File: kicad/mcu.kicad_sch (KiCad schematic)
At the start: 1 part, among them U12 ESP32-S3-WROOM-1-N8R2

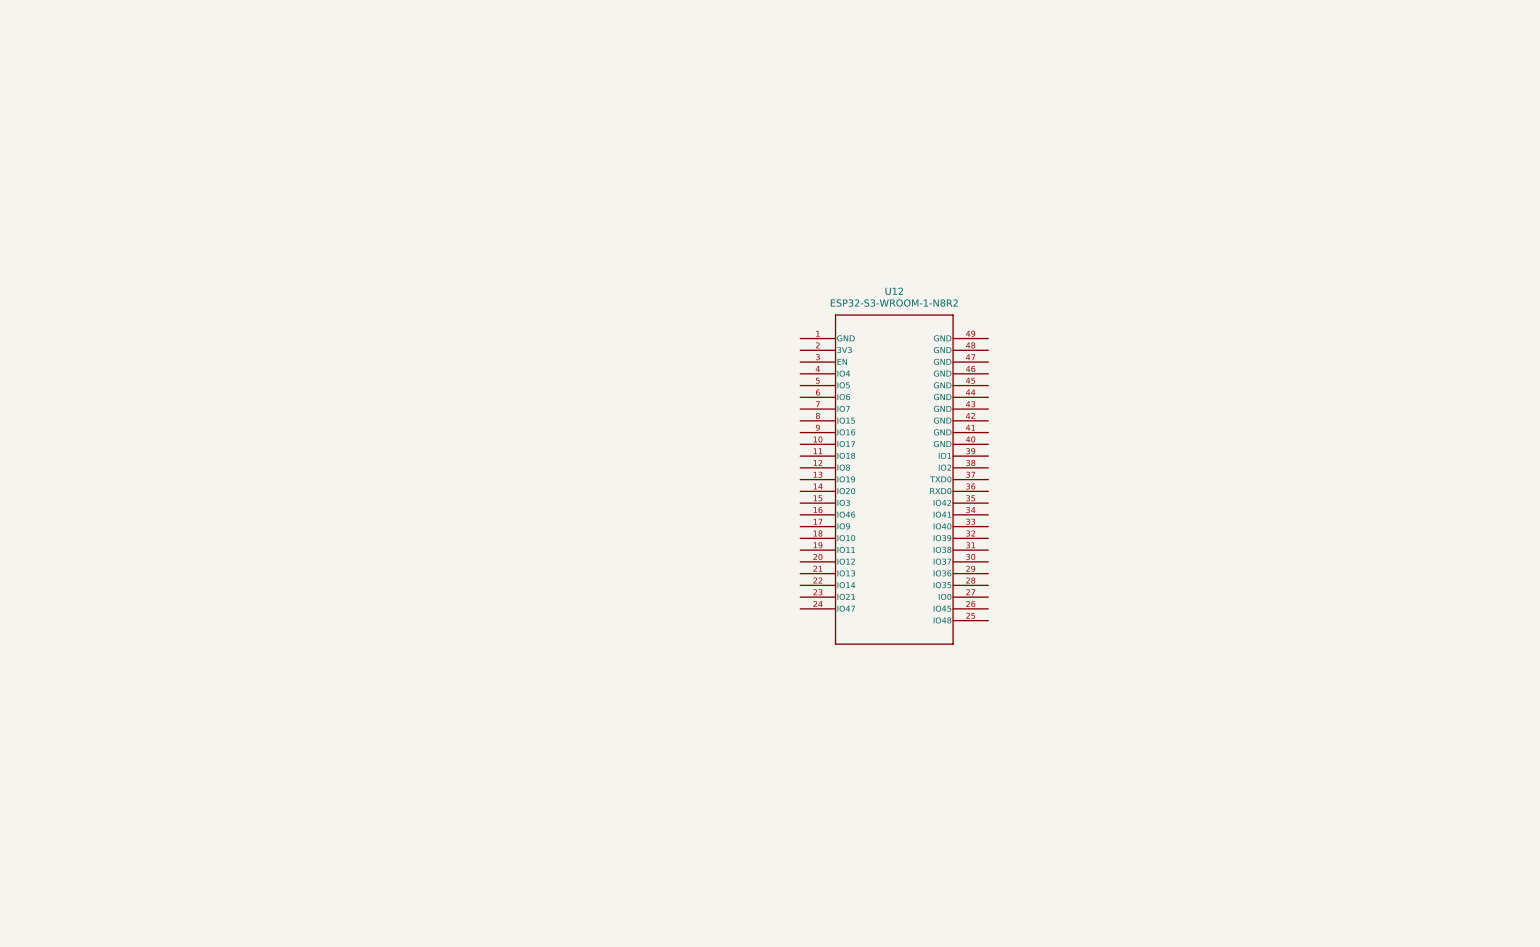
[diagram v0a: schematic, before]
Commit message: wire up mcu
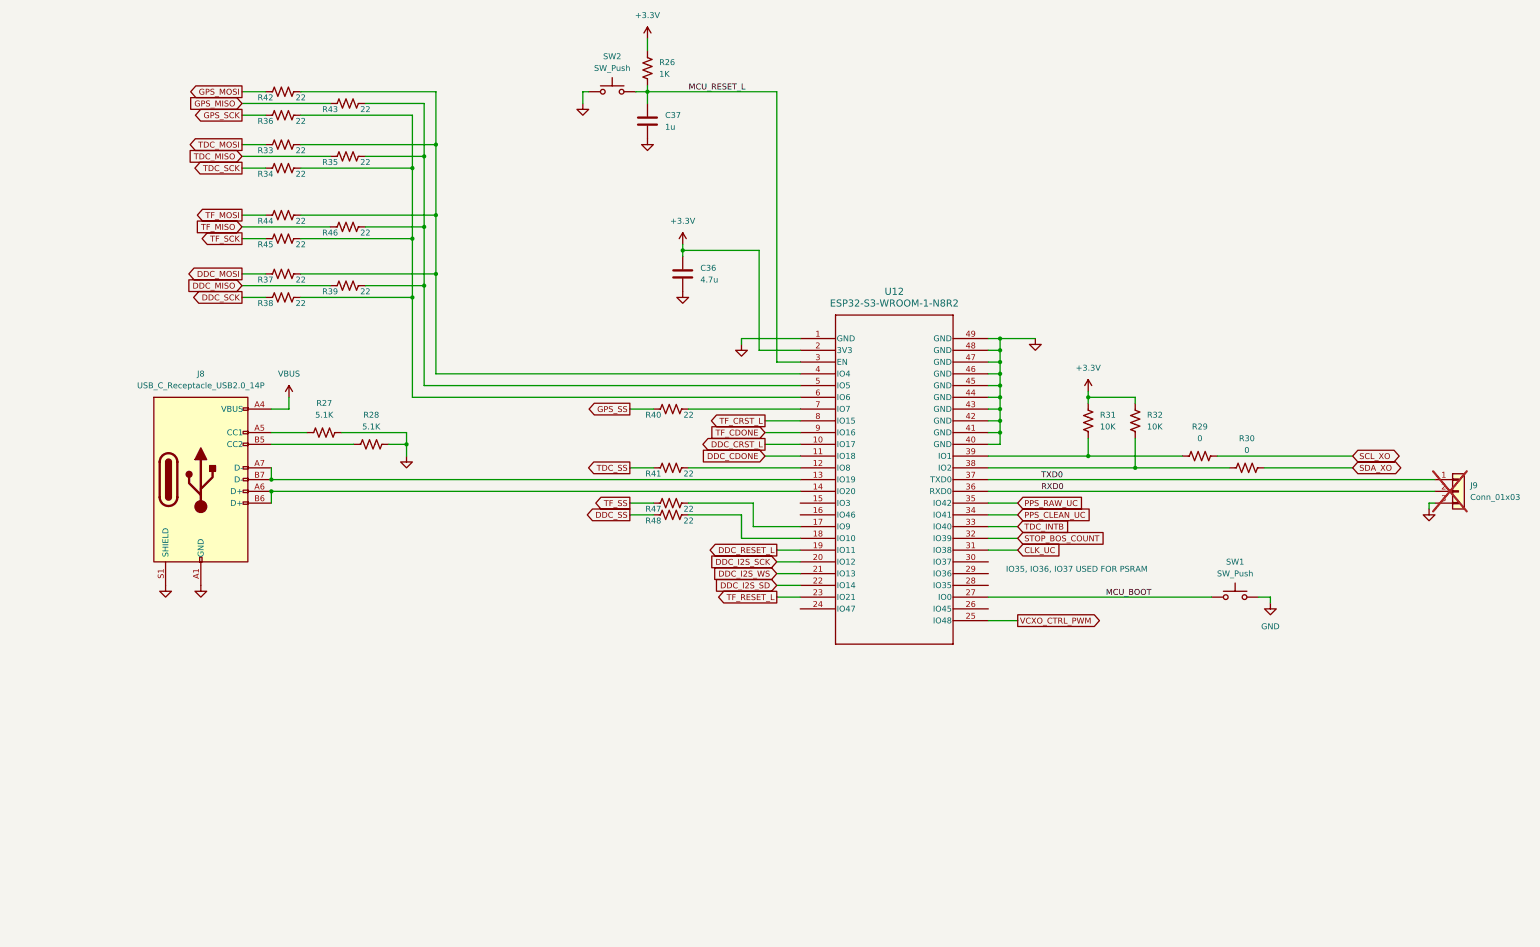
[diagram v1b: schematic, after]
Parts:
- added C36: 4.7u, symbol Device:C
- added C37: 1u, symbol Device:C
- added J8: USB_C_Receptacle_USB2.0_14P, symbol Connector:USB_C_Receptacle_USB2.0_14P
- added J9: Conn_01x03, symbol Connector_Generic:Conn_01x03
- added R26: 1K, symbol Device:R_US
- added R27, R28: 5.1K, symbol Device:R_US
- added R29, R30: 0, symbol Device:R_US
- added R31, R32: 10K, symbol Device:R_US
- added R33, R34, R35, R36, R37, R38, R39, R40, R41, R42, R43, R44, R45, R46, R47, R48: 22, symbol Device:R_US
- added SW1, SW2: SW_Push, symbol Switch:SW_Push
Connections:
- net GND: now reaches U12.1 (GND)
- net GND: now also U12.40 (GND), U12.41 (GND), U12.42 (GND), U12.43 (GND), U12.44 (GND), U12.45 (GND), U12.46 (GND), U12.47 (GND), U12.48 (GND), U12.49 (GND), C36.2, C37.2, J8.A1 (GND), J8.A12 (GND), J8.B1 (GND), J8.B12 (GND), J8.S1 (SHIELD), J9.3 (Pin_3), R27.2, R28.2, SW1.2, SW2.1
- net DDC_CRST_L: now reaches U12.10 (IO17)
- net DDC_CDONE: now reaches U12.11 (IO18)
- net at U12.12 (IO8): now also R41.2
- net at U12.13 (IO19): now also J8.A7 (D-), J8.B7 (D-)
- net at U12.14 (IO20): now also J8.A6 (D+), J8.B6 (D+)
- net at U12.17 (IO9): now also R47.2
- net at U12.18 (IO10): now also R48.2
- net DDC_RESET_L: now reaches U12.19 (IO11)
- net +3.3V: now reaches U12.2 (3V3)
- net +3.3V: now also C36.1, R26.1, R31.1, R32.1
- net DDC_I2S_SCK: now reaches U12.20 (IO12)
- net DDC_I2S_WS: now reaches U12.21 (IO13)
- net DDC_I2S_SD: now reaches U12.22 (IO14)
- net TF_RESET_L: now reaches U12.23 (IO21)
- net VCXO_CTRL_PWM: now reaches U12.25 (IO48)
- net MCU_BOOT: now reaches U12.27 (IO0)
- net MCU_BOOT: now also SW1.1
- net MCU_RESET_L: now reaches U12.3 (EN)
- net MCU_RESET_L: now also C37.1, R26.2, SW2.2
- net CLK_UC: now reaches U12.31 (IO38)
- net STOP_BOS_COUNT: now reaches U12.32 (IO39)
- net TDC_INTB: now reaches U12.33 (IO40)
- net PPS_CLEAN_UC: now reaches U12.34 (IO41)
- net PPS_RAW_UC: now reaches U12.35 (IO42)
- net RXD0: now reaches U12.36 (RXD0)
- net RXD0: now also J9.2 (Pin_2)
- net TXD0: now reaches U12.37 (TXD0)
- net TXD0: now also J9.1 (Pin_1)
- net at U12.38 (IO2): now also R30.1, R32.2
- net at U12.39 (IO1): now also R29.1, R31.2
- net at U12.4 (IO4): now also R33.2, R37.2, R42.2, R44.2
- net at U12.5 (IO5): now also R35.2, R39.2, R43.2, R46.2
- net at U12.6 (IO6): now also R34.2, R36.2, R38.2, R45.2
- net at U12.7 (IO7): now also R40.2
- net TF_CRST_L: now reaches U12.8 (IO15)
- net TF_CDONE: now reaches U12.9 (IO16)
- new net: J8.A5 (CC1), R27.1
- new net: J8.B5 (CC2), R28.1
- new net DDC_MISO: R39.1
- new net DDC_MOSI: R37.1
- new net DDC_SCK: R38.1
- new net DDC_SS: R48.1
- new net GPS_MISO: R43.1
- new net GPS_MOSI: R42.1
- new net GPS_SCK: R36.1
- new net GPS_SS: R40.1
- new net SCL_XO: R29.2
- new net SDA_XO: R30.2
- new net TDC_MISO: R35.1
- new net TDC_MOSI: R33.1
- new net TDC_SCK: R34.1
- new net TDC_SS: R41.1
- new net TF_MISO: R46.1
- new net TF_MOSI: R44.1
- new net TF_SCK: R45.1
- new net TF_SS: R47.1
- new net VBUS: J8.A4 (VBUS), J8.A9 (VBUS), J8.B4 (VBUS), J8.B9 (VBUS)
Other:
- note added: "IO35, IO36, IO37 USED FOR PSRAM"

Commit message: fix ercs
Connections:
- net CLK_UC: now also U12.26 (IO45); no longer U12.31 (IO38)
- net STOP_BOS_COUNT: now also U12.33 (IO40); no longer U12.32 (IO39)
- net TDC_INTB: now also U12.32 (IO39); no longer U12.33 (IO40)
- net GPS_RESET_L: now reaches U12.24 (IO47)
- new net TDC_EN: U12.31 (IO38)
- no-connect marks 0 -> 5
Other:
- note added: "NOTE: IO45 IS A BOOTSTRAP. ANY ISSUE?"

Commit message: bos/tos tweaks
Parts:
- added R49, R50: 0, symbol Device:R_US
- R31, R32: value 10K -> 4.7K
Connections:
- net SCL_UC: now reaches R29.1, R31.2, U12.39 (IO1)
- net SCL_UC: now also R49.1
- net SPI_SCK_UC: now reaches R34.2, R36.2, R38.2, R45.2, U12.6 (IO6)
- net SDA_UC: now reaches R30.1, R32.2, U12.38 (IO2)
- net SDA_UC: now also R50.1
- net SPI_MOSI_UC: now reaches R33.2, R37.2, R42.2, R44.2, U12.4 (IO4)
- net SPI_MISO_UC: now reaches R35.2, R39.2, R43.2, R46.2, U12.5 (IO5)
- net STOP_BOS_COUNT renamed STOP_TOS_COUNT
- new net SCL_TEMP: R49.2
- new net SDA_TEMP: R50.2
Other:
- moved on the sheet: R29, R30
